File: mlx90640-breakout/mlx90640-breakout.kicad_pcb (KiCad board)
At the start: 2 copper layers, 12.7 x 25.4 mm, 10 parts, among them J1 Conn_01x04_Male, U1 MLX90640, U2 MLX90640

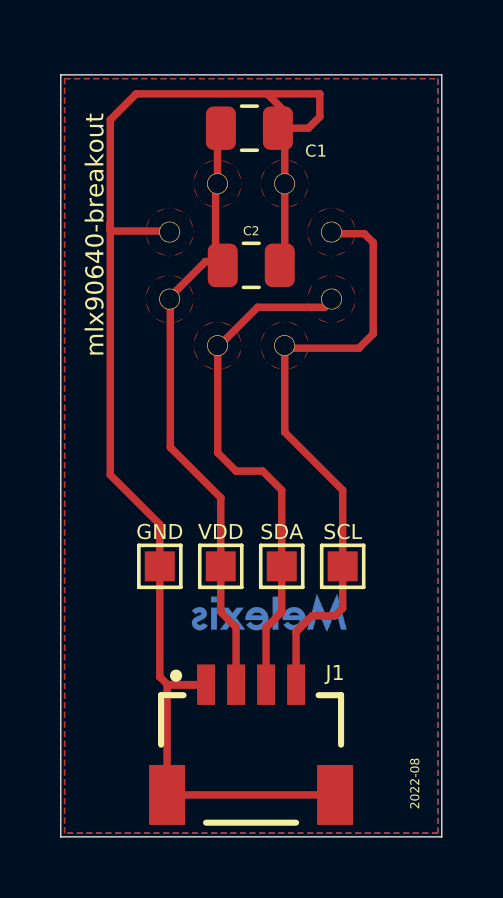
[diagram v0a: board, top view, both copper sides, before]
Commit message: updated breakout boards
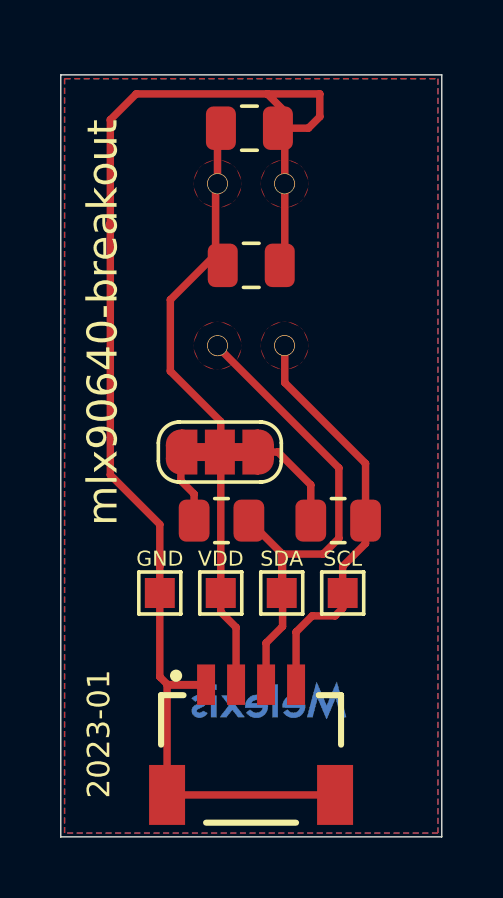
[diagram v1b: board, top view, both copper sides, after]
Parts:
- removed U2: MLX90640, melexis-temperature:mlx90640_41
- added JP1: SolderJumper_3_Bridged123, Jumper:SolderJumper-3_P1.3mm_Bridged12_RoundedPad1.0x1.5mm_NumberLabels, F.Cu at (109.9, 70.7)
- added R1: 4K7, Resistor_SMD:R_0805_2012Metric, F.Cu at (113.8, 73.0)
- added R2: 4K7, Resistor_SMD:R_0805_2012Metric, F.Cu at (110.0, 73.0)
- moved G*** 2.92 mm to (110.9, 78.9)
- moved GND 0.89 mm to (107.9, 75.4)
- moved SCL 0.89 mm to (114.0, 75.4)
- moved SDA 0.89 mm to (112.0, 75.4)
- moved VDD 0.89 mm to (109.9, 75.4)
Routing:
- net /SCL: track 20.8 -> 13.8 mm
- net Net-(JP1-Pad3): track 0.00 -> 3.37 mm
- net Net-(JP1-Pad1): track 0.00 -> 2.47 mm
- net /GND: track 49.3 -> 47.3 mm
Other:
- board text added: "2023-01"
- board text added: "MLX90640"
- board text added: "MLX90641"
- board text removed: "2022-08"
